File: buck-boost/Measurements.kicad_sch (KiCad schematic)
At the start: 0 parts

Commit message: Adding supply block
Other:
- note added: "[1]"
- note added: "[1] Vdd: 5V"
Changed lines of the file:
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@@
+		)
+	)
+	(text "[1] Vdd: 5V"
+		(exclude_from_sim no)
+		(at 183.134 151.638 0)
+		(effects
+			(font
+				(size 1.27 1.27)
+			)
 		)
 	)
@@
 		(effects
 			(font
+				(size 1.27 1.27)
+			)
+		)
+	)
+	(text "[1]"
+		(exclude_from_sim no)
+		(at 21.336 177.038 0)
+		(effects
+			(font

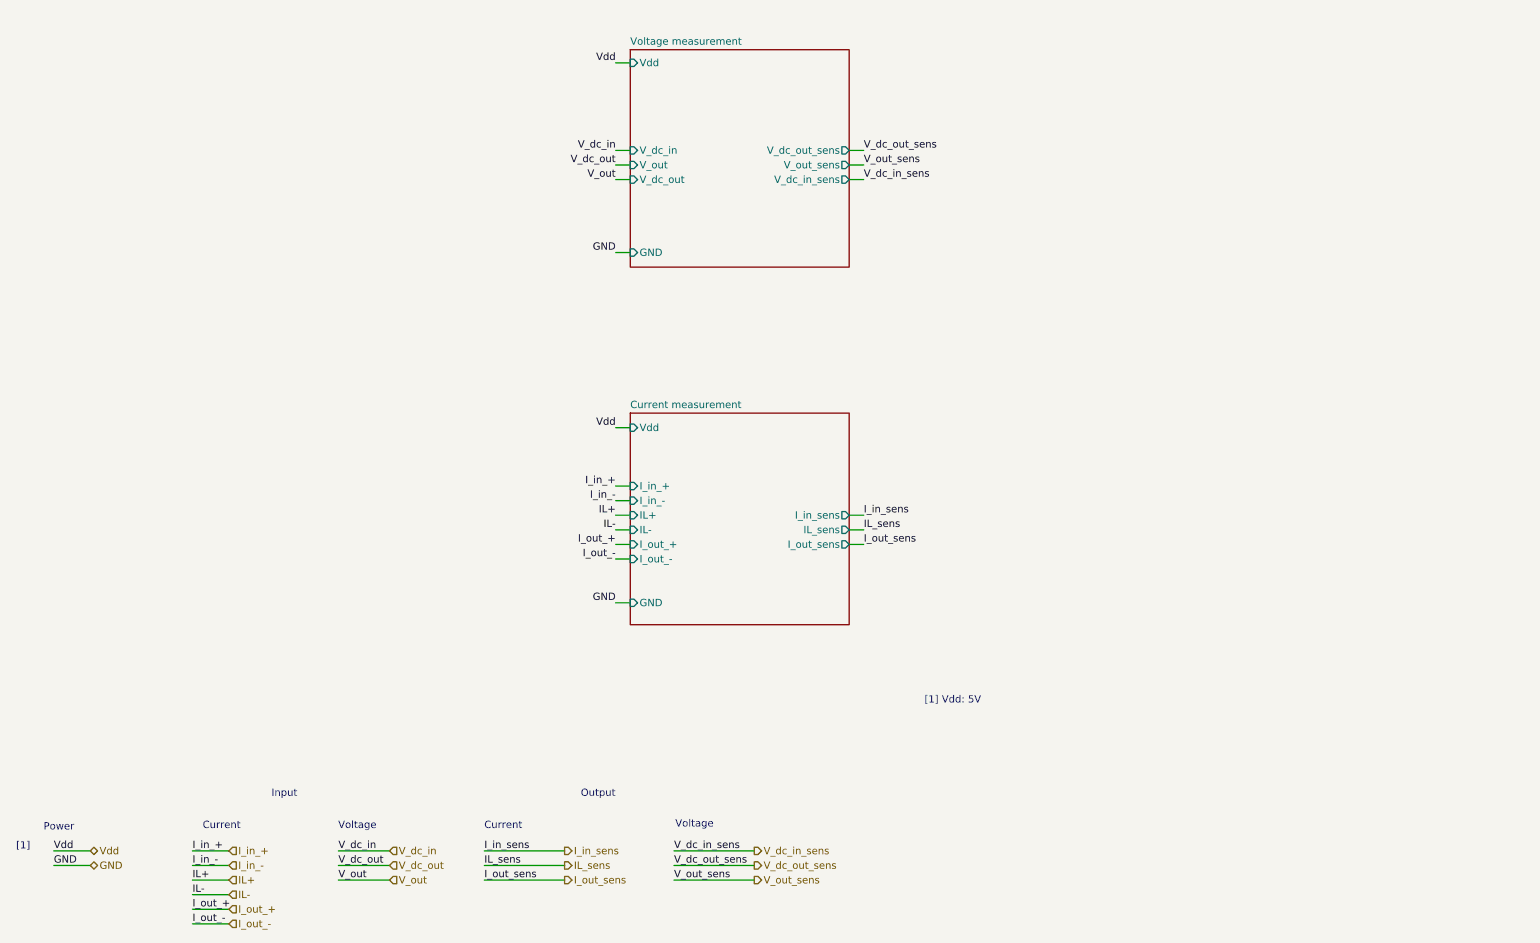
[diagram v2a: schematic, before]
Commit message: The changes indicated in the text document Review. 05.11.2024 were implemented. Missing footprints were added
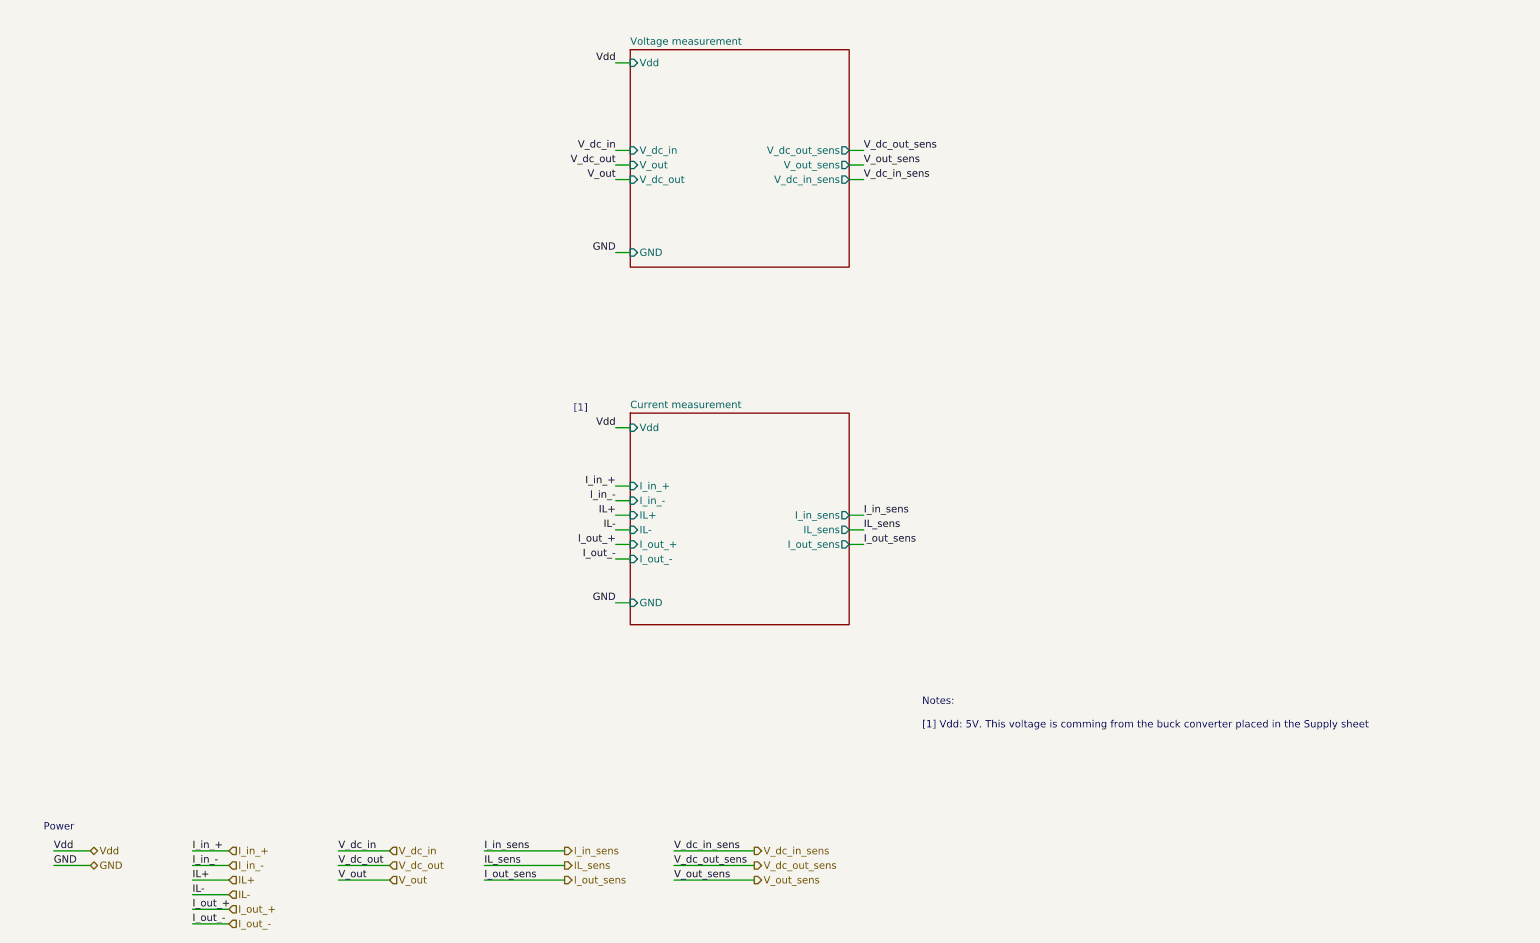
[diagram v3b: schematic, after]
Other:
- note added: "Notes: [1] Vdd: 5V. This voltage is comming from the buck converter placed in the Supply sheet"
- note removed: "Current"
- note removed: "Input"
- note removed: "Output"
- note removed: "Voltage"
- note removed: "[1] Vdd: 5V"
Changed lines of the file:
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@@
 		)
 	)
-	(text "[1] Vdd: 5V"
+	(text "Notes:\n\n[1] Vdd: 5V. This voltage is comming from the buck converter placed in the Supply sheet "
 		(exclude_from_sim no)
-		(at 183.134 151.638 0)
+		(at 177.8 153.924 0)
 		(effects
 			(font
 				(size 1.27 1.27)
 			)
-		)
-	)
-	(text "Voltage"
-		(exclude_from_sim no)
-		(at 138.176 173.228 0)
-		(effects
-			(font
-				(size 1.27 1.27)
-			)
-		)
-	)
-	(text "Voltage"
-		(exclude_from_sim no)
-		(at 79.502 173.482 0)
-		(effects
-			(font
-				(size 1.27 1.27)
-			)
-		)
-	)
-	(text "Current"
-		(exclude_from_sim no)
-		(at 104.902 173.482 0)
-		(effects
-			(font
-				(size 1.27 1.27)
-			)
-		)
-	)
-	(text "Input\n"
-		(exclude_from_sim no)
-		(at 66.802 167.894 0)
-		(effects
-			(font
-				(size 1.27 1.27)
-			)
+			(justify left)
 		)
 	)
@@
 		)
 	)
-	(text "Current"
+	(text "[1]"
 		(exclude_from_sim no)
-		(at 55.88 173.482 0)
+		(at 118.364 100.838 0)
 		(effects
 			(font
-				(size 1.27 1.27)
-			)
-		)
-	)
-	(text "Output\n"
-		(exclude_from_sim no)
-		(at 121.412 167.894 0)
-		(effects
-			(font
-				(size 1.27 1.27)
-			)
-		)
-	)
-	(text "[1]"
-		(exclude_from_sim no)
-		(at 21.336 177.038 0)
-		(effects
-			(font

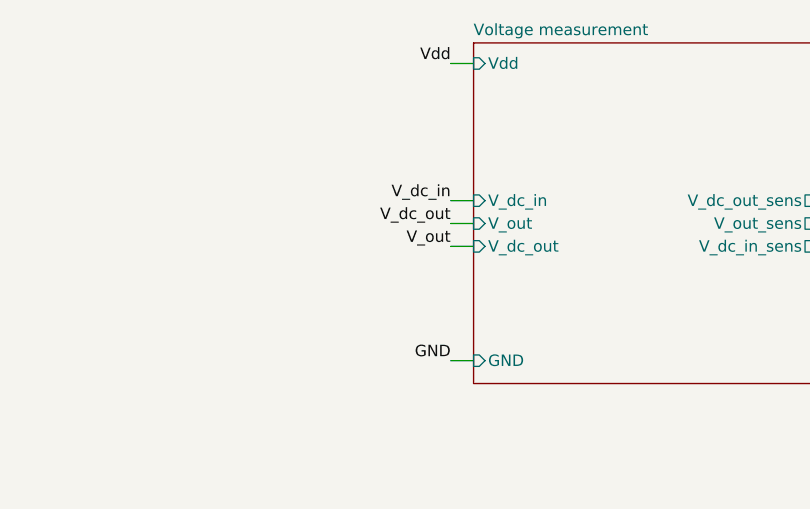
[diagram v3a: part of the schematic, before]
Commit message: Some errors in the schematics were corrected. PCB file V1.0
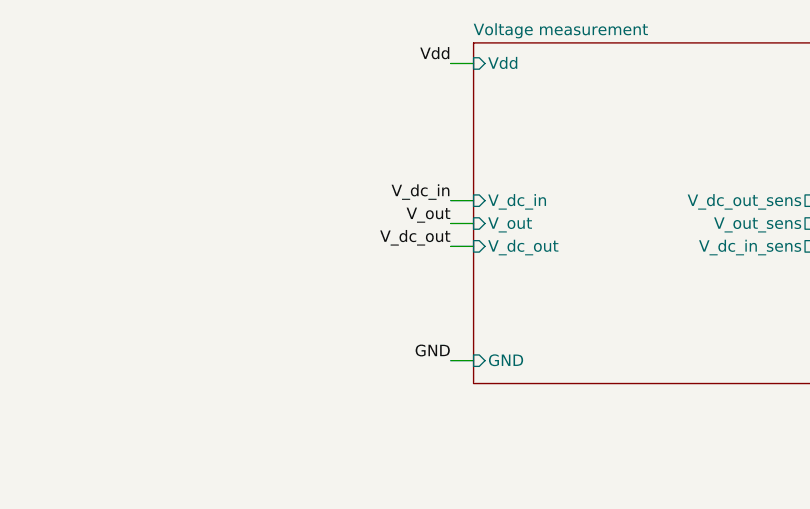
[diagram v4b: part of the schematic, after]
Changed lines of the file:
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@@
 	)
 	(label "V_out"
-		(at 124.46 60.96 180)
+		(at 124.46 58.42 180)
 		(fields_autoplaced yes)
 		(effects
@@
 	)
 	(label "V_dc_out"
-		(at 124.46 58.42 180)
-		(fields_autoplaced yes)
-		(effects
+		(at 124.46 60.96 180)
+		(fields_autoplaced yes)
+		(effects
